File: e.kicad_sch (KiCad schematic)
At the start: 9 parts, among them SW1 usr, SW2 rst, U1 Display_ST7789, U2 MAX98357A

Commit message: i made a fatal mistake..
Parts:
- BT1: value CR2430 -> CR2450
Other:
- note added: "switched from 2032 to 2430 because of the way the 2430 battery hold is designed, its lowkey impossible to wire it backwards, eliminating the need for schottky diode. edit: bc of the pico, we need it for extra safety :( edit edit: I ORDERED THE PCB WITH THE 2450 FOOTPRINT BY MISTAKE q-q"
- note removed: "switched from 2032 to 2430 because of the way the 2430 battery hold is designed, its lowkey impossible to wire it backwards, eliminating the need for schottky diode. edit: bc of the pico, we need it for extra safety :("
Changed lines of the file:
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@@
 		)
 	)
-	(text "switched from 2032 to 2430 because of\nthe way the 2430 battery hold is designed, \nits lowkey impossible to wire it backwards, \neliminating the need for schottky diode.\n\nedit: bc of the pico, we need it for extra safety :("
+	(text "switched from 2032 to 2430 because of\nthe way the 2430 battery hold is designed, \nits lowkey impossible to wire it backwards, \neliminating the need for schottky diode.\n\nedit: bc of the pico, we need it for extra safety :(\nedit edit: I ORDERED THE PCB WITH THE 2450 FOOTPRINT BY MISTAKE q-q"
 		(exclude_from_sim no)
-		(at 49.53 45.212 0)
+		(at 52.07 53.086 0)
 		(effects
 			(font
@@
 			)
 		)
-		(property "Value" "CR2430"
+		(property "Value" "CR2450"
 			(at 83.82 33.7184 0)
 			(show_name no)

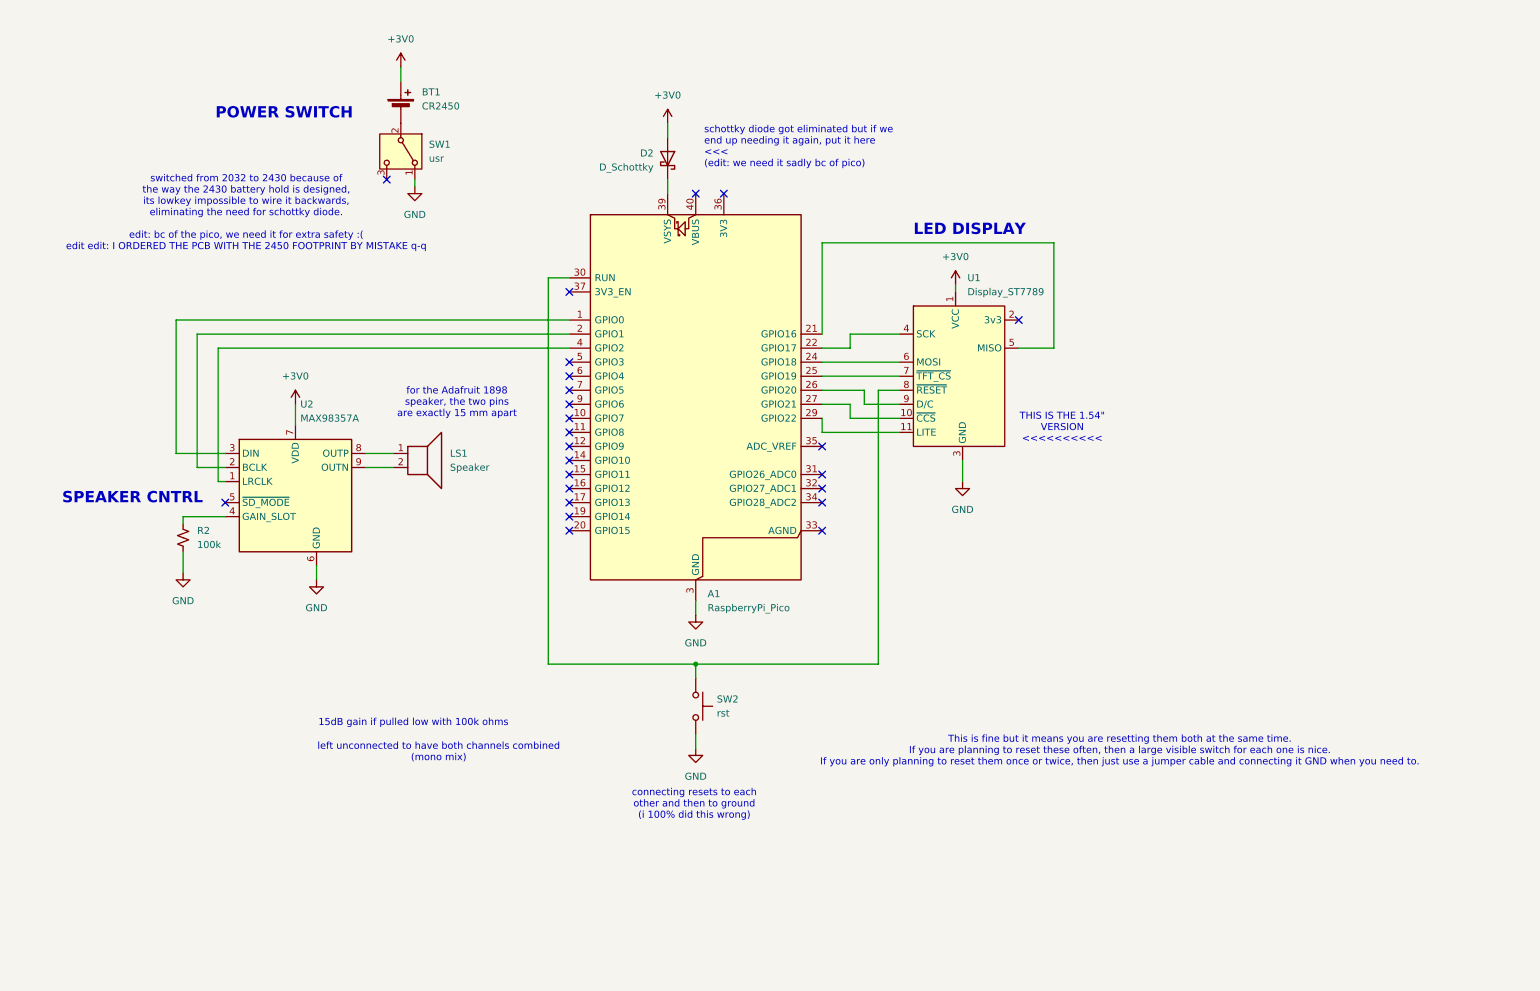
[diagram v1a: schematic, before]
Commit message: schematic redone
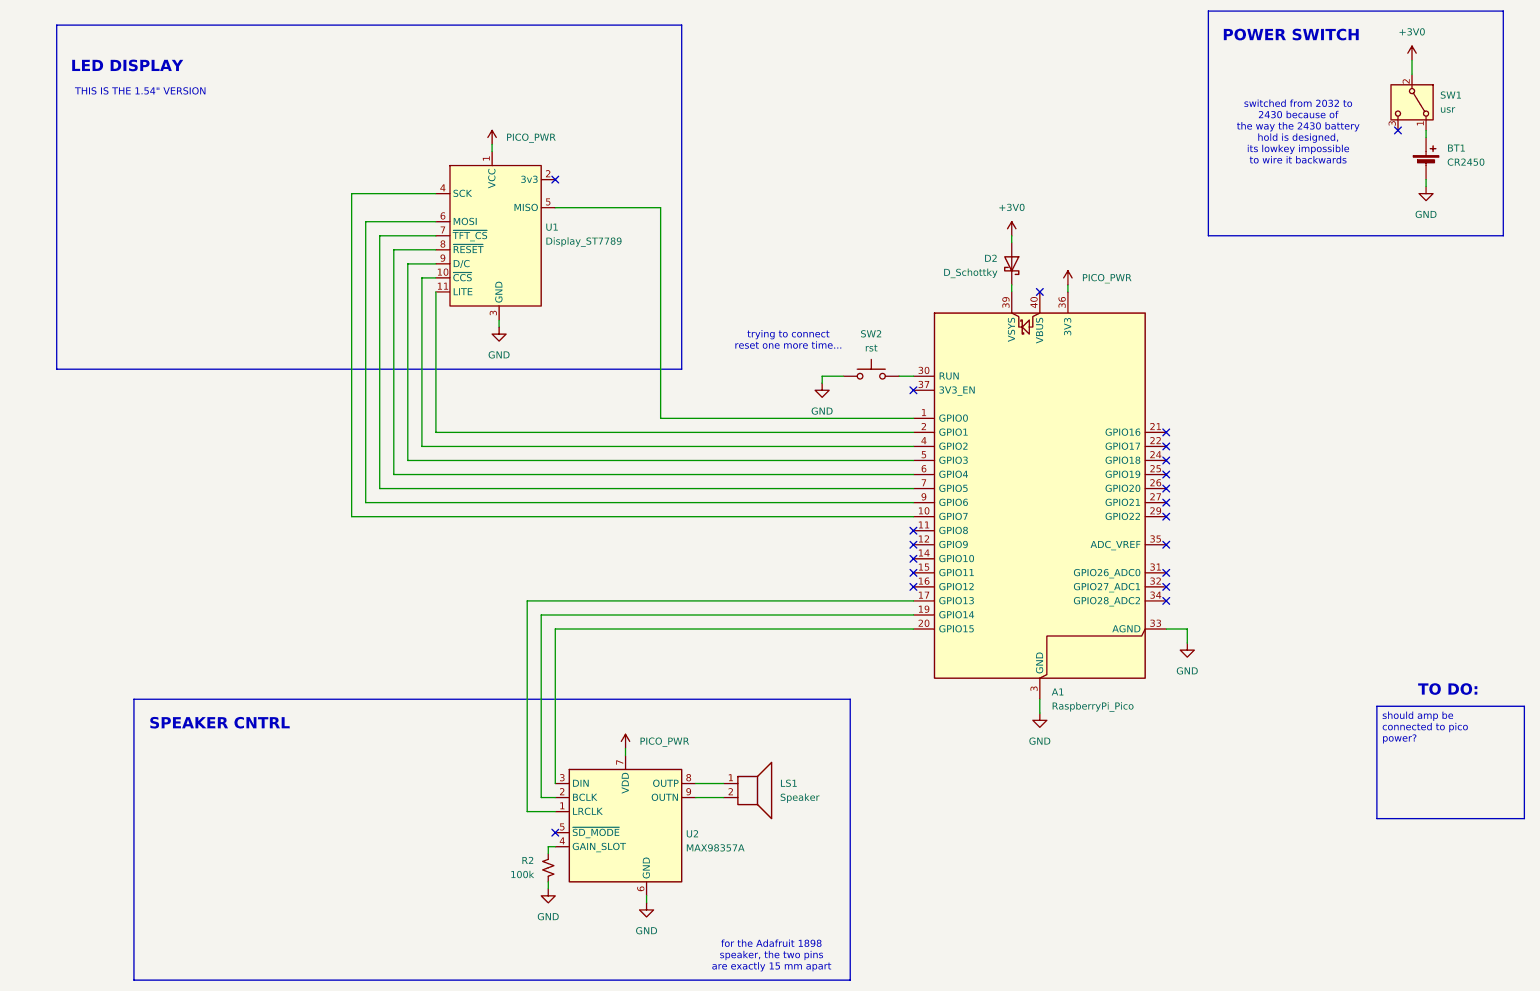
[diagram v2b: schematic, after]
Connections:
- net +3V0: now also SW1.2 (B); no longer BT1.1 (+), U1.1 (VCC), U2.7 (VDD)
- net GND: now also A1.33 (AGND), BT1.2 (-), SW2.1; no longer SW1.1 (A), SW2.2
- net at A1.1 (GPIO0): now also U1.5 (MISO); no longer U2.3 (DIN)
- net at A1.10 (GPIO7): now also U1.4 (SCK)
- net at A1.17 (GPIO13): now also U2.1 (LRCLK)
- net at A1.19 (GPIO14): now also U2.2 (BCLK)
- net at A1.2 (GPIO1): now also U1.11 (LITE); no longer U2.2 (BCLK)
- net at A1.20 (GPIO15): now also U2.3 (DIN)
- net at A1.21 (GPIO16): no longer U1.5 (MISO)
- net at A1.22 (GPIO17): no longer U1.4 (SCK)
- net at A1.24 (GPIO18): no longer U1.6 (MOSI)
- net at A1.25 (GPIO19): no longer U1.7 (~{TFT_CS})
- net at A1.26 (GPIO20): no longer U1.9 (D/C)
- net at A1.27 (GPIO21): no longer U1.10 (~{CCS})
- net at A1.29 (GPIO22): no longer U1.11 (LITE)
- net PICO_PWR: now reaches A1.36 (3V3)
- net PICO_PWR: now also U1.1 (VCC), U2.7 (VDD)
- net at A1.4 (GPIO2): now also U1.10 (~{CCS}); no longer U2.1 (LRCLK)
- net at A1.5 (GPIO3): now also U1.9 (D/C)
- net at A1.6 (GPIO4): now also U1.8 (~{RESET})
- net at A1.7 (GPIO5): now also U1.7 (~{TFT_CS})
- net at A1.9 (GPIO6): now also U1.6 (MOSI)
- new net: A1.30 (RUN), SW2.2
- new net: BT1.1 (+), SW1.1 (A)
- no-connect marks 24 -> 21
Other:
- note added: "THIS IS THE 1.54" VERSION"
- note added: "TO DO:"
- note added: "switched from 2032 to 2430 because of the way the 2430 battery hold is designed, its lowkey impossible to wire it backwards"
- note added: "trying to connect reset one more time..."
- note removed: "15dB gain if pulled low with 100k ohms"
- note removed: "THIS IS THE 1.54" VERSION <<<<<<<<<<"
- note removed: "This is fine but it means you are resetting them both at the same time. If you are planning to reset these often, then a large visible switch for each one is nice. If you are only planning to reset them once or twice, then just use a jumper cable and connecting it GND when you need to."
- note removed: "connecting resets to each other and then to ground (i 100% did this wrong)"
- note removed: "left unconnected to have both channels combined (mono mix)"
- note removed: "schottky diode got eliminated but if we end up needing it again, put it here <<< (edit: we need it sadly bc of pico)"
- note removed: "switched from 2032 to 2430 because of the way the 2430 battery hold is designed, its lowkey impossible to wire it backwards, eliminating the need for schottky diode. edit: bc of the pico, we need it for extra safety :( edit edit: I ORDERED THE PCB WITH THE 2450 FOOTPRINT BY MISTAKE q-q"
- moved on the sheet: A1, D2, LS1, R2, SW1, U2

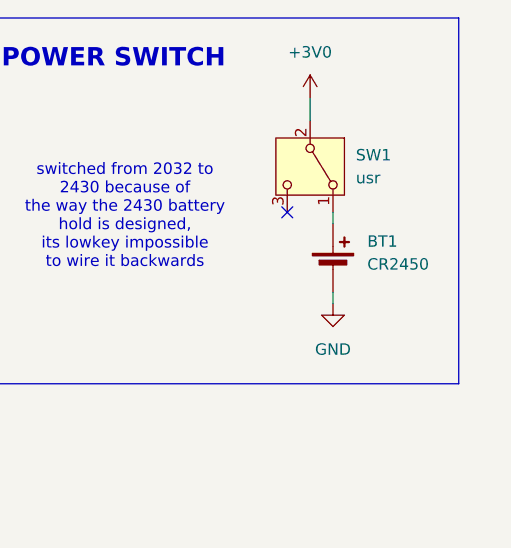
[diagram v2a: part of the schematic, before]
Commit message: corrected battery + picked new footprints
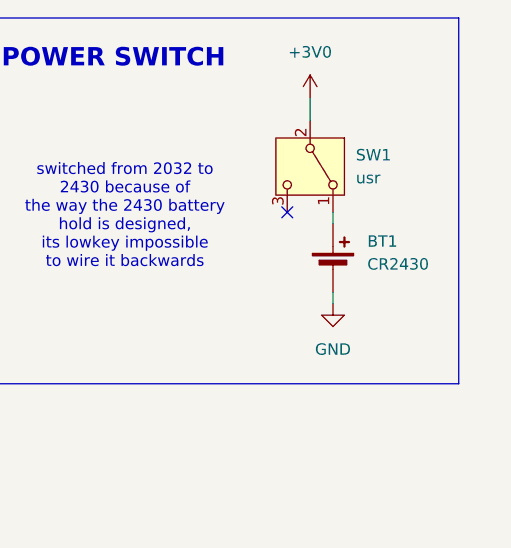
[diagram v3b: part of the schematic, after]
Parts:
- A1: footprint Module:RaspberryPi_Pico_Common_Unspecified -> Module:RaspberryPi_Pico_Common_SMD
- BT1: value CR2450 -> CR2430; footprint Battery:BatteryHolder_Keystone_3008_1x2450 -> Battery:BatteryHolder_Keystone_105_1x2430
- D2: footprint Diode_SMD:D_SOD-323 -> Diode_SMD:D_SOD-128
- R2: footprint Resistor_SMD:R_1206_3216Metric -> Resistor_SMD:R_1812_4532Metric
- SW2: footprint Button_Switch_SMD:SW_Push_1P1T_NO_CK_KMR2 -> Button_Switch_SMD:SW_Push_1P1T_NO_CK_KSC9xxG
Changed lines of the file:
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@@
 			)
 		)
-		(property "Footprint" "Module:RaspberryPi_Pico_Common_Unspecified"
+		(property "Footprint" "Module:RaspberryPi_Pico_Common_SMD"
 			(at 195.58 152.4 0)
 			(hide yes)
@@
 			)
 		)
-		(property "Value" "CR2450"
+		(property "Value" "CR2430"
 			(at 269.24 43.8784 0)
 			(show_name no)
@@
 			)
 		)
-		(property "Footprint" "Battery:BatteryHolder_Keystone_3008_1x2450"
+		(property "Footprint" "Battery:BatteryHolder_Keystone_105_1x2430"
 			(at 265.43 42.926 90)
 			(hide yes)
@@
 			)
 		)
-		(property "Footprint" "Diode_SMD:D_SOD-323"
+		(property "Footprint" "Diode_SMD:D_SOD-128"
 			(at 190.5 62.23 0)
 			(hide yes)
@@
 			)
 		)
-		(property "Footprint" "Resistor_SMD:R_1206_3216Metric"
+		(property "Footprint" "Resistor_SMD:R_1812_4532Metric"
 			(at 106.68 171.45 0)
 			(hide yes)
@@
 			)
 		)
-		(property "Footprint" "Button_Switch_SMD:SW_Push_1P1T_NO_CK_KMR2"
+		(property "Footprint" "Button_Switch_SMD:SW_Push_1P1T_NO_CK_KSC9xxG"
 			(at 165.1 77.47 0)
 			(hide yes)

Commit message: pcb layout done!!
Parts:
- BT1: value CR2430 -> CR2450; footprint Battery:BatteryHolder_Keystone_105_1x2430 -> Battery:BatteryHolder_Keystone_3008_1x2450
- SW2: footprint Button_Switch_SMD:SW_Push_1P1T_NO_CK_KSC9xxG -> Button_Switch_SMD:SW_Push_SPST_NO_Alps_SKRK
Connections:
- net at A1.17 (GPIO13): now also U2.3 (DIN); no longer U2.1 (LRCLK)
- net at A1.20 (GPIO15): now also U2.1 (LRCLK); no longer U2.3 (DIN)
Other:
- note removed: "switched from 2032 to 2430 because of the way the 2430 battery hold is designed, its lowkey impossible to wire it backwards"
- moved on the sheet: BT1, SW1

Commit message: mfw i cant find one part so i have to change the entire board
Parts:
- R2: footprint Resistor_SMD:R_1812_4532Metric -> Resistor_THT:R_Axial_DIN0207_L6.3mm_D2.5mm_P10.16mm_Horizontal
- SW2: footprint Button_Switch_SMD:SW_Push_SPST_NO_Alps_SKRK -> Button_Switch_THT:SW_PUSH_6mm
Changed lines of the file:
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@@
 			)
 		)
-		(property "Footprint" "Resistor_SMD:R_1812_4532Metric"
+		(property "Footprint" "Resistor_THT:R_Axial_DIN0207_L6.3mm_D2.5mm_P10.16mm_Horizontal"
 			(at 106.68 171.45 0)
 			(hide yes)
@@
 			)
 		)
-		(property "Footprint" "Button_Switch_SMD:SW_Push_SPST_NO_Alps_SKRK"
+		(property "Footprint" "Button_Switch_THT:SW_PUSH_6mm"
 			(at 165.1 77.47 0)
 			(hide yes)
